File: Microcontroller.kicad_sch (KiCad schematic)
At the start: 36 parts, among them IC201 ESP32-S3-WROOM-1-N4, SW201 NRST, SW202 USER, SW203 USER, SW204 USER, U201 STM32F405RGTx, Y201 16MHz|9p|10ppm

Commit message: Prawie skończone
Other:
- note added: "- Zintegrować wyprowadzenia z modułami Adama?"
- note added: "TO DO"
- note added: "[3] Microcontroller & WIFI module"
- note removed: "[2] Microcontroller & WIFI module"
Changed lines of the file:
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@@
     (stroke (width 0) (type default))
+  )
+  (rectangle (start 340.36 17.78) (end 393.7 63.5)
+    (stroke (width 0.5) (type default) (color 255 14 41 1))
+    (fill (type none))
   )
   (rectangle (start 19.05 44.45) (end 192.278 233.934)
@@
     (fill (type none))
   )
-  (rectangle (start 207.01 44.196) (end 380.238 233.68)
+  (rectangle (start 207.01 68.58) (end 380.238 233.68)
     (stroke (width 0) (type dash))
     (fill (type none))
@@
     (fill (type none))
   )
-  (text "ESP32_WIFI_MODULE" (at 210.566 51.816 0)
+  (text "ESP32_WIFI_MODULE" (at 215.9 78.74 0)
     (effects (font (size 3 3) (thickness 0.6) bold) (justify left bottom))
   )
@@
     (effects (font (size 0.6 0.6)) (justify left bottom))
   )
-  (text "[2] Microcontroller & WIFI module\n" (at 17.526 25.908 0)
+  (text "- Zintegrować wyprowadzenia\n z modułami Adama? " (at 342.9 33.02 0)
+    (effects (font (size 2 2)) (justify left bottom))
+  )
+  (text "[3] Microcontroller & WIFI module\n" (at 17.526 25.908 0)
     (effects (font (size 5 5) (thickness 1) bold) (justify left bottom))
   )
+  (text "TO DO " (at 342.8328 23.7686 0)
+    (effects (font (size 3 3) (thickness 0.6) bold) (justify left bottom))
+  )
   (text "CL1,2 = 2(CL - CS) \n" (at 54.61 177.038 0)

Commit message: Dodaje wszystko nie chce mi sie z tym bawic
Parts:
- removed C201, C202: 2u2, symbol Device:C_Small
- removed C203, C205, C211, C213, C218, C219, C220, C221, C222, C223: 100n, Capacitor_SMD:C_0402_1005Metric, symbol Device:C_Small
- removed C204: 10u, Capacitor_SMD:C_0603_1608Metric, symbol Device:C_Small
- removed C209, C210: 10p, Capacitor_SMD:C_0402_1005Metric, symbol Device:C_Small
- removed C212: 1u, Capacitor_SMD:C_0603_1608Metric, symbol Device:C_Small
- removed C217: 4u7, Capacitor_SMD:C_0603_1608Metric, symbol Device:C_Small
- removed D201, D202: LED_WHITE, Diode_SMD:D_0603_1608Metric, symbol Device:LED
- removed FB201: Optionally, symbol Device:FerriteBead_Small
- removed IC201: ESP32-S3-WROOM-1-N4, ESP32S3WROOM1N4, symbol SamacSys_Parts:ESP32-S3-WROOM-1-N4
- removed R201: 22, Resistor_SMD:R_0402_1005Metric, symbol Device:R
- removed R202: 10k, Resistor_SMD:R_0402_1005Metric, symbol Device:R
- removed R203, R206: 1k, Resistor_SMD:R_0603_1608Metric, symbol Device:R_Small
- removed R204, R205: R_Small, symbol Device:R_Small
- removed R207: 0, symbol Device:R_Small
- removed SW201: NRST, Button_Switch_SMD:SW_Push_1P1T_NO_6x6mm_H9.5mm, symbol Switch:SW_MEC_5G
- removed SW202, SW203: USER, Button_Switch_SMD:SW_Push_1P1T_NO_6x6mm_H9.5mm, symbol Switch:SW_MEC_5G
- removed U201: STM32F405RGTx, Package_QFP:LQFP-64_10x10mm_P0.5mm, symbol MCU_ST_STM32F4:STM32F405RGTx
- removed Y201: 16MHz|9p|10ppm, Crystal:Crystal_SMD_3225-4Pin_3.2x2.5mm, symbol Device:Crystal_GND24_Small
- added C302, C303, C304, C306, C314, C318, C320, C322, C324, C325, C326: 100n, Capacitor_SMD:C_0603_1608Metric, symbol Device:C_Small
- added C305: 047u, Capacitor_SMD:C_0603_1608Metric, symbol Device:C_Small
- added C313, C316: 10p, Capacitor_SMD:C_0603_1608Metric, symbol Device:C_Small
- added C315: 1u, Capacitor_SMD:C_0603_1608Metric, symbol Device:C_Small
- added C317: 10n, Capacitor_SMD:C_0603_1608Metric, symbol Device:C_Small
- added C319: 4u7, Capacitor_SMD:C_0603_1608Metric, symbol Device:C_Small
- added C321, C323: 2u2, Capacitor_SMD:C_0603_1608Metric, symbol Device:C_Small
- added D301, D302, D304: LED_WHITE, Diode_SMD:D_0603_1608Metric, symbol Device:LED
- added D602: D_Schottky, Adam_lib:D_SOD-123FL, symbol Device:D_Schottky
- added FB302: Optionally, Inductor_SMD:L_0603_1608Metric, symbol Device:FerriteBead_Small
- added J301: Conn_02x05_Counter_Clockwise, symbol Connector_Generic:Conn_02x05_Counter_Clockwise
- added R302, R303: 10k, Resistor_SMD:R_0603_1608Metric, symbol Device:R
- added R304, R309, R310: 1k, Resistor_SMD:R_0603_1608Metric, symbol Device:R_Small
- added R305, R306: R_Small, Resistor_SMD:R_0603_1608Metric, symbol Device:R_Small
- added R307: 22, Resistor_SMD:R_0603_1608Metric, symbol Device:R
- added SW302, SW304: USER, Button_Switch_SMD:SW_Push_1P1T_NO_6x6mm_H9.5mm, symbol Switch:SW_MEC_5G
- added SW303: NRST, Button_Switch_SMD:SW_Push_1P1T_NO_6x6mm_H9.5mm, symbol Switch:SW_MEC_5G
- added SW601: SW_SPDT, symbol Switch:SW_SPDT
- added U302: STM32F405RGT6, Package_QFP:LQFP-64_10x10mm_P0.5mm, symbol MCU_ST_STM32F4:STM32F405RGTx
- added Y302: 16MHz|9p|10ppm, Crystal:Crystal_SMD_3225-4Pin_3.2x2.5mm, symbol Device:Crystal_GND24_Small
- C206: footprint Capacitor_SMD:C_0402_1005Metric -> Capacitor_SMD:C_0603_1608Metric
- R208: footprint (none) -> Resistor_SMD:R_0603_1608Metric
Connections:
- net +3.3V: now also C305.1, C315.1, C319.1, C320.1, C322.1, C324.1, C325.1, C326.1, FB302.1, SW601.3 (C), U302.1 (VBAT), U302.19 (VDD), U302.32 (VDD), U302.48 (VDD), U302.64 (VDD)
- net +3.3VA: now also C306.1, C317.1, FB302.2, U302.13 (VDDA)
- net GND: now also C302.2, C303.1, C304.2, C305.2, C306.2, C313.1, C313.2, C314.2, C315.2, C316.2, C317.2, C318.1, C319.2, C320.2, C321.2, C322.2, C323.2, C324.2, C325.2, C326.2, D301.1 (K), D302.1 (K), D304.1 (K), J301.3 (Pin_3), J301.8 (Pin_8), SW302.3 (B), SW302.4 (B), SW303.3 (B), SW303.4 (B), SW304.3 (B), SW304.4 (B), SW601.1 (A), U302.12 (VSSA), U302.18 (VSS), U302.5 (PH0), U302.63 (VSS), Y302.1, Y302.2, Y302.4
- net HSE OUT: now also C316.1, R307.2, Y302.3
- net HSE_OUT: now also R307.1, U302.6 (PH1)
- net NRST: now also C314.1, D602.2 (A), R302.1, R302.2, SW303.1 (A), SW303.2 (A), U302.7 (NRST)
- net USER_B: now also C302.1, R305.2, U302.29 (PB10)
- net USER_B2: now also C303.2, R306.1, U302.30 (PB11)
- net USER_LD: now also R309.1, U302.33 (PB12)
- net USER_LD2: now also R310.1, U302.34 (PB13)
- net USER_LD2_A: now also D302.2 (A), R310.2
- net USER_LD_A: now also D301.2 (A), R309.2
- new net: C318.2, R306.2, SW304.1 (A), SW304.2 (A)
- new net: C304.1, R305.1, SW302.1 (A), SW302.2 (A)
- new net: D602.1 (K), J301.1 (Pin_1)
- new net: C321.1, U302.31 (VCAP_1)
- new net: C323.1, U302.47 (VCAP_2)
- new net: R303.2, U302.60 (BOOT0)
- new net: R303.1, SW601.2 (B)
- new net 5V_ST: J301.5 (Pin_5), J301.6 (Pin_6)
- new net BMI088_INT1_ACC: U302.2 (PC13)
- new net BMI088_INT3_GYRO: U302.3 (PC14)
- new net I2C1_SCK: U302.61 (PB8)
- new net I2C1_SDA: U302.62 (PB9)
- new net IR_1: U302.41 (PA8)
- new net IR_2: U302.42 (PA9)
- new net IR_3: U302.43 (PA10)
- new net IR_4: U302.44 (PA11)
- new net IR_5: U302.23 (PA7)
- new net IR_6: U302.22 (PA6)
- new net REC_1: U302.14 (PA0)
- new net REC_2: U302.15 (PA1)
- new net REC_3: U302.16 (PA2)
- new net REC_4: U302.17 (PA3)
- new net REC_5: U302.20 (PA4)
- new net REC_6: U302.21 (PA5)
- new net SPI1_CS_ESP: U302.28 (PB2)
- new net SPI1_MISO_ESP: U302.56 (PB4)
- new net SPI1_MOSI_ESP: U302.57 (PB5)
- new net SPI1_SCK: U302.55 (PB3)
- new net SWCLK: J301.10 (Pin_10), U302.49 (PA14)
- new net SWDIO: J301.9 (Pin_9), U302.46 (PA13)
- new net TIM_ENCODER_A1: U302.26 (PB0)
- new net TIM_ENCODER_A2: U302.58 (PB6)
- new net TIM_ENCODER_B1: U302.27 (PB1)
- new net TIM_ENCODER_B2: U302.59 (PB7)
- new net UART4_RX: U302.52 (PC11)
- new net UART4_TX: U302.51 (PC10)
- new net UART5_RX: U302.54 (PD2)
- new net UART5_TX: U302.53 (PC12)
- new net USER_LD3: R304.1, U302.35 (PB14)
- new net USER_LD3_A: D304.2 (A), R304.2
- no-connect marks 0 -> 17
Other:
- note added: "Drawn by: Adam Iwachów"
- note added: "Encoders"
- note added: "HSE"
- note added: "IR DIODES TX PWM"
- note added: "Optionally"
- note added: "PHOTO RX ADC"
- note added: "STATUS LED"
- note added: "STM have internal pull up"
- note added: "SWD"
- note added: "USER BUTTON"
- note added: "nRST"
- note removed: "- Zintegrować wyprowadzenia z modułami Adama?"
- note removed: "BOOT0 provides three ways of booting program into stm32, when pull down, we can simply use ST-LINK witw serial wire debub, when pull high, we can upload program by usb"
- note removed: "Internal ldo decoupling cap. If package have only one Vcap pin Vcap = 4.7uF, where ESR < 1ohm"
- note removed: "TO DO"
- moved on the sheet: C206, R208, SW204

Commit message: footprinty
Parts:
- J301: footprint (none) -> Connector_PinHeader_2.54mm:PinHeader_2x05_P2.54mm_Vertical
- SW601: footprint (none) -> Button_Switch_THT:SW_PUSH_1P1T_6x3.5mm_H4.3_APEM_MJTP1243
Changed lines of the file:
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@@
       (effects (font (size 1.27 1.27)))
     )
-    (property "Footprint" "" (at 198.12 220.98 0)
+    (property "Footprint" "Connector_PinHeader_2.54mm:PinHeader_2x05_P2.54mm_Vertical" (at 198.12 220.98 0)
       (effects (font (size 1.27 1.27)) hide)
     )
@@
       (effects (font (size 1.27 1.27)))
     )
-    (property "Footprint" "" (at 106.68 114.3 0)
-      (effects (font (size 1.27 1.27)) hide)
-    )
+    (property "Footprint" "Button_Switch_THT:SW_PUSH_1P1T_6x3.5mm_H4.3_APEM_MJTP1243" (at 106.68 114.3 0)
+      (effects (font (size 1.27 1.27)) hide)
+    )

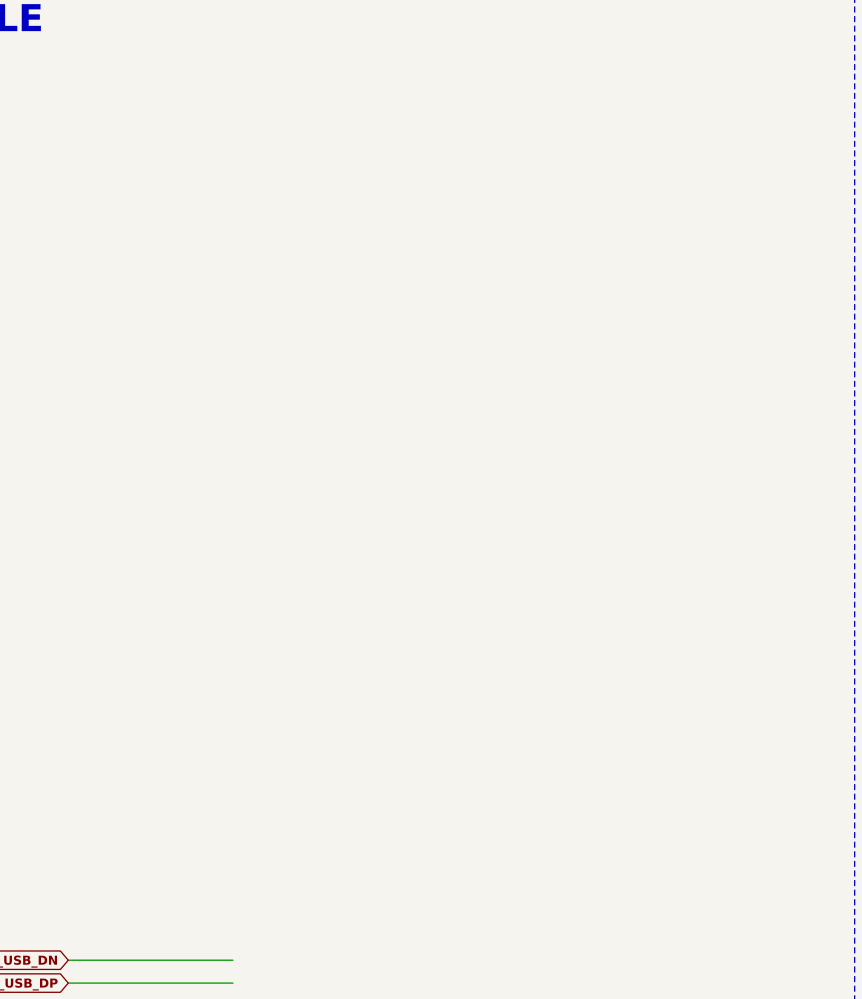
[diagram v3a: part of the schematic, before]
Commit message: wstępnie zrobiony adapter ESP32-S3. oceń czy jest git to zrobię footprinta do niego
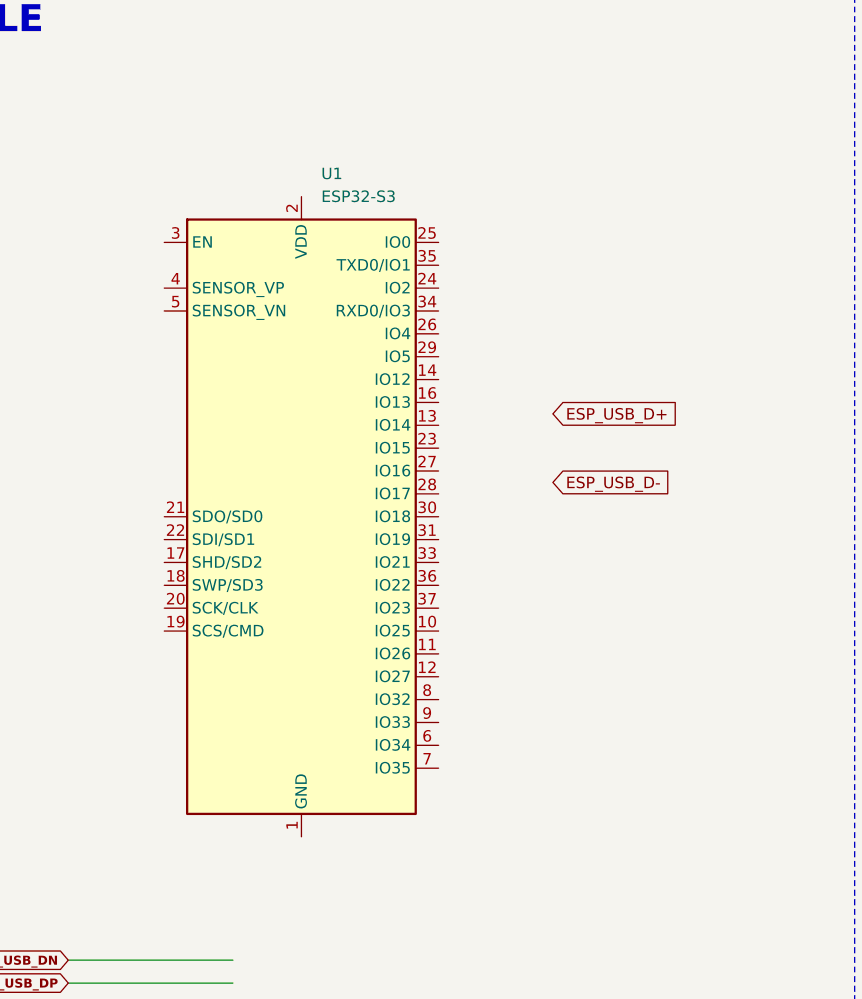
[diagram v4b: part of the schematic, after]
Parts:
- added U1: ESP32-S3, KoNaR_STANDARDY:adapter_ESP32, symbol RF_Module:ESP32-WROOM-32U
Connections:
- new net: U1.1 (GND), U1.15 (GND), U1.38 (GND), U1.39 (GND)
